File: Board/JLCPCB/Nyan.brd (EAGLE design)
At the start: 86 x 42 mm, 63 parts, among them IC1 74HCT541PW, IC2 STM32F10XCXT6, IC3 74HCT541PW, IC4 ST3485, U2 A4988_STEP, U3 MAX6966, X1 WR-WTB2.0-2_THT-VER, X10 32768, X2 WR-WTB2.0-4_THT_VER, X3 WR-WTB2.0-5_THT-VER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

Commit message: [Board] A little more layouting done
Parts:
- removed SV1: (no value), con-lstb:MA03-2
- added JP1, JP2: (no value), jumper:JP1
- moved LED1 32.3 mm to (54.2, 14.7), turned to 180 degrees
- moved R9 30.1 mm to (54.5, 17.9), turned to 90 degrees
- moved X9 28.9 mm to (24.1, 12.8), turned to 0 degrees
- moved C10 25.9 mm to (23.1, 16.2)
- moved C9 24.6 mm to (22.9, 9.65)
- moved X10 23.3 mm to (29.9, 11.1)
- moved C7 20.2 mm to (1.25, 2.60), flipped to the top
- moved C11 19.4 mm to (26.9, 8.20)
- moved C12 16.6 mm to (30.6, 8.40), turned to 0 degrees
- moved C18 14.4 mm to (50.0, 3.10)
- moved C16 14.4 mm to (45.0, 3.10)
- moved C17 14.4 mm to (47.4, 2.90)
- moved C19 13.8 mm to (52.0, 2.90)
- moved C15 13.8 mm to (42.5, 3.10)
- moved R5 13.3 mm to (2.90, 2.90), flipped to the top
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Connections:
- removed net N$12: R6.2, SV1.2
- removed net N$13: R7.2, SV1.1
- net +3V3: now also JP1.2, JP2.2; no longer SV1.5, SV1.6
- net BOOT1: now also JP2.1, R6.2; no longer SV1.4
- net N$7: now also JP1.1, R7.2; no longer SV1.3

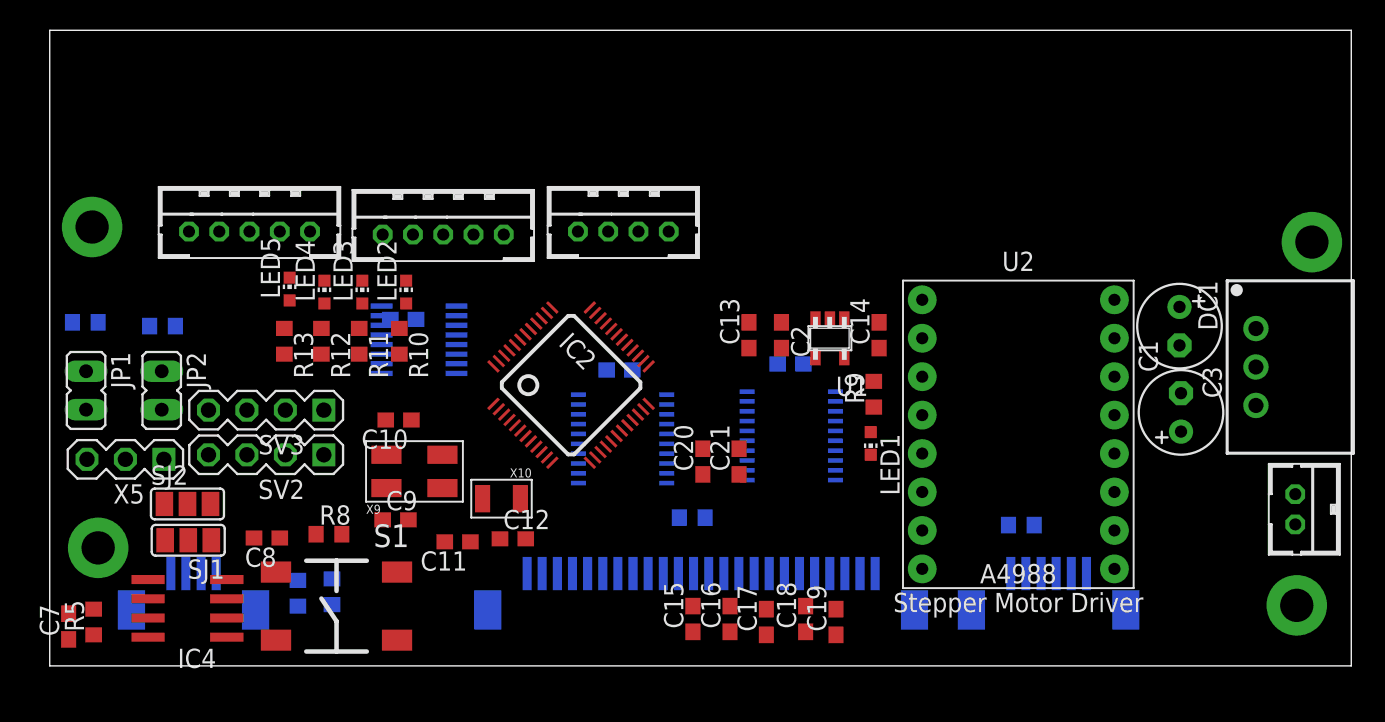
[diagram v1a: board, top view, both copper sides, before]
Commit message: [Board] Positioning done
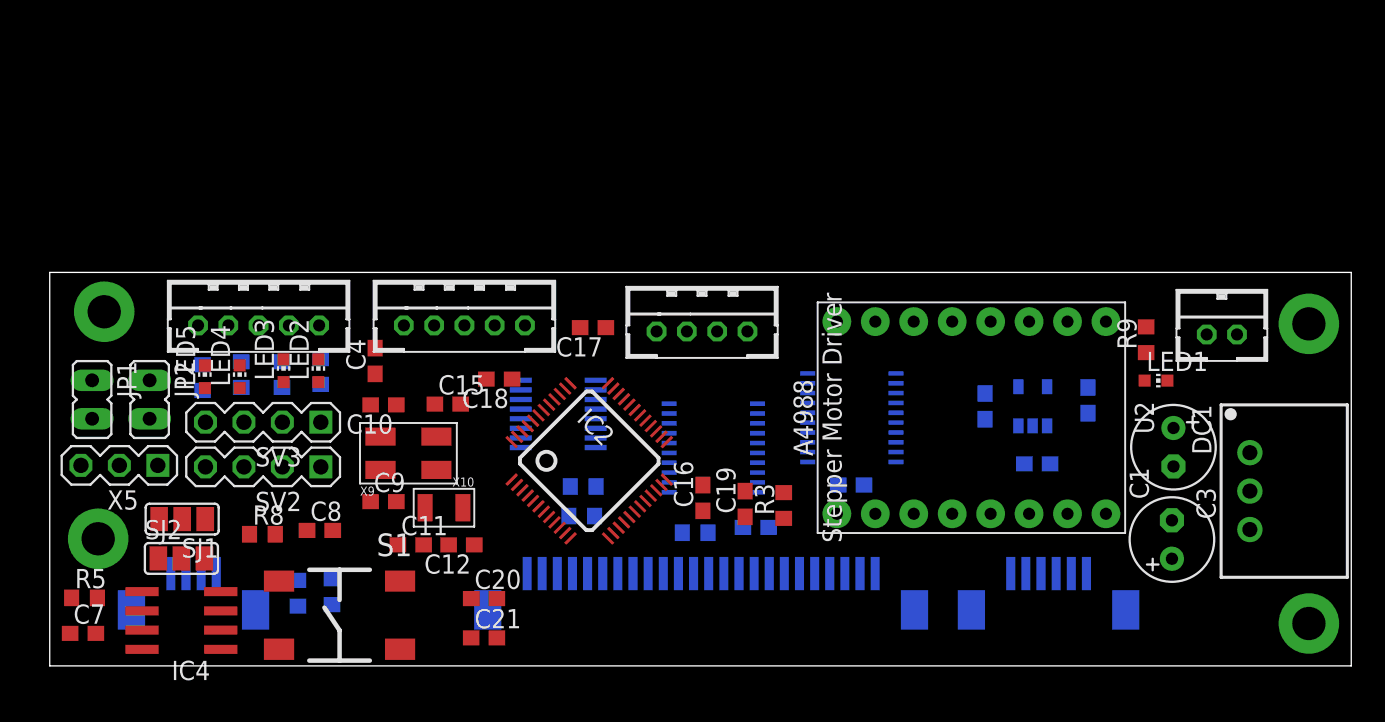
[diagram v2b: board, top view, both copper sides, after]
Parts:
- moved R7 35.2 mm to (35.1, 9.90)
- moved R6 29.8 mm to (35.2, 11.8)
- moved C18 25.7 mm to (29.7, 18.9), turned to 180 degrees
- moved C17 22.6 mm to (35.9, 22.4), turned to 180 degrees
- moved C15 21.5 mm to (26.3, 17.3), turned to 0 degrees
- moved C21 20.5 mm to (28.7, 1.85), turned to 0 degrees
- moved LED1 19.3 mm to (73.1, 18.9), turned to 270 degrees
- moved C2 18.9 mm to (65.2, 13.3), flipped to the bottom, turned to 0 degrees
- moved R9 18.4 mm to (72.5, 21.6)
- moved C20 17.1 mm to (28.7, 4.45), turned to 0 degrees
- moved C13 16.3 mm to (61.8, 17.1), flipped to the bottom, turned to 270 degrees
- moved R3 15.8 mm to (48.5, 10.6), flipped to the top, turned to 90 degrees
- moved X4 15.5 mm to (27.4, 22.5)
- moved C14 14.5 mm to (68.6, 17.6), flipped to the bottom, turned to 270 degrees
- moved U1 14.1 mm to (65.0, 17.1), flipped to the bottom, turned to 0 degrees
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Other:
- board size 86 x 42 mm -> 86 x 26 mm

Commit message: [Board] Fixed positions for half the components
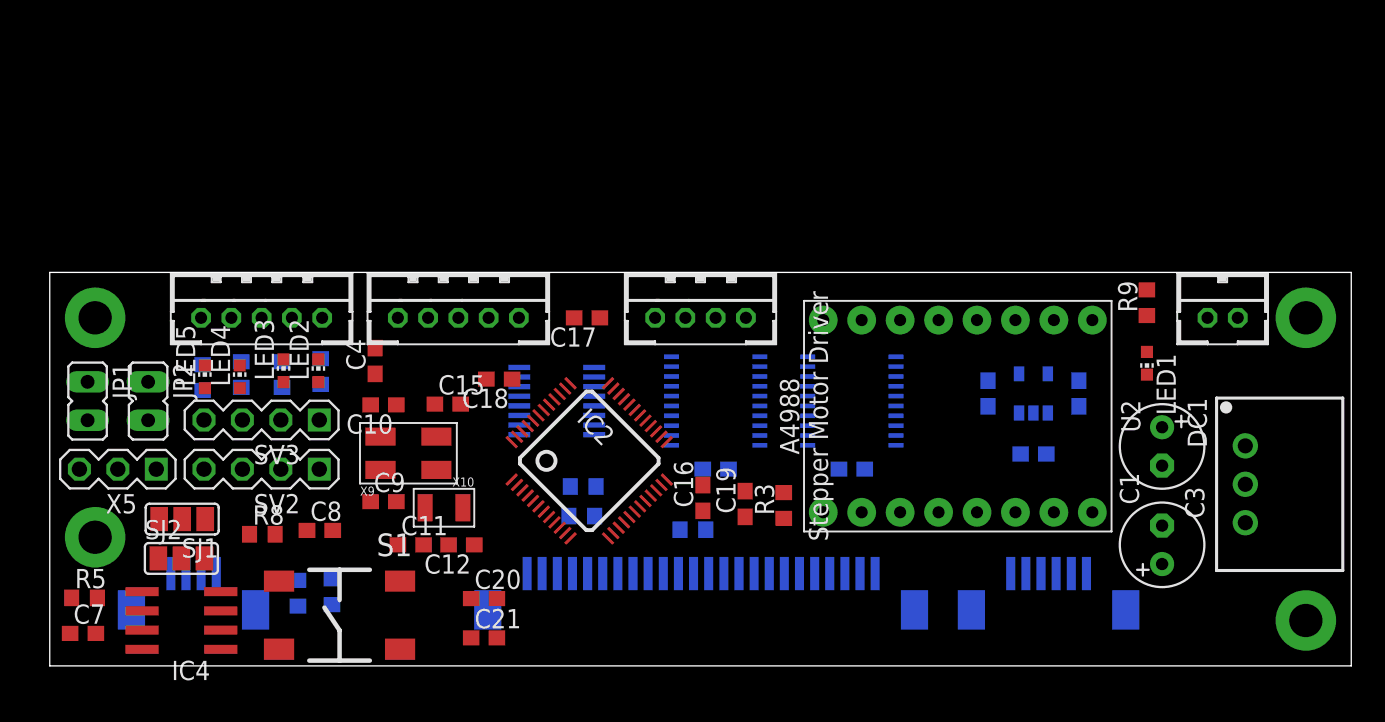
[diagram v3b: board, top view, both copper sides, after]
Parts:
- moved C5 4.67 mm to (44.0, 13.0)
- moved IC3 3.10 mm to (44.0, 17.5)
- moved R9 2.45 mm to (72.5, 24.0)
- moved LED1 1.30 mm to (72.5, 20.0), turned to 180 degrees
- moved X1 1.10 mm to (77.5, 23.0)
- moved IC1 1.10 mm to (53.0, 17.5)
- moved C6 1.05 mm to (53.0, 13.0)
- moved U2 0.91 mm to (60.0, 16.5)
- moved X2 0.91 mm to (43.0, 23.0)
- moved C13 0.87 mm to (62.0, 18.0)
- moved U3 0.86 mm to (33.5, 17.5)
- moved U1 0.85 mm to (65.0, 18.0)
- moved C17 0.76 mm to (35.5, 23.0)
- moved C3 0.75 mm to (73.5, 14.5)
- moved C14 0.75 mm to (68.0, 18.0)
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
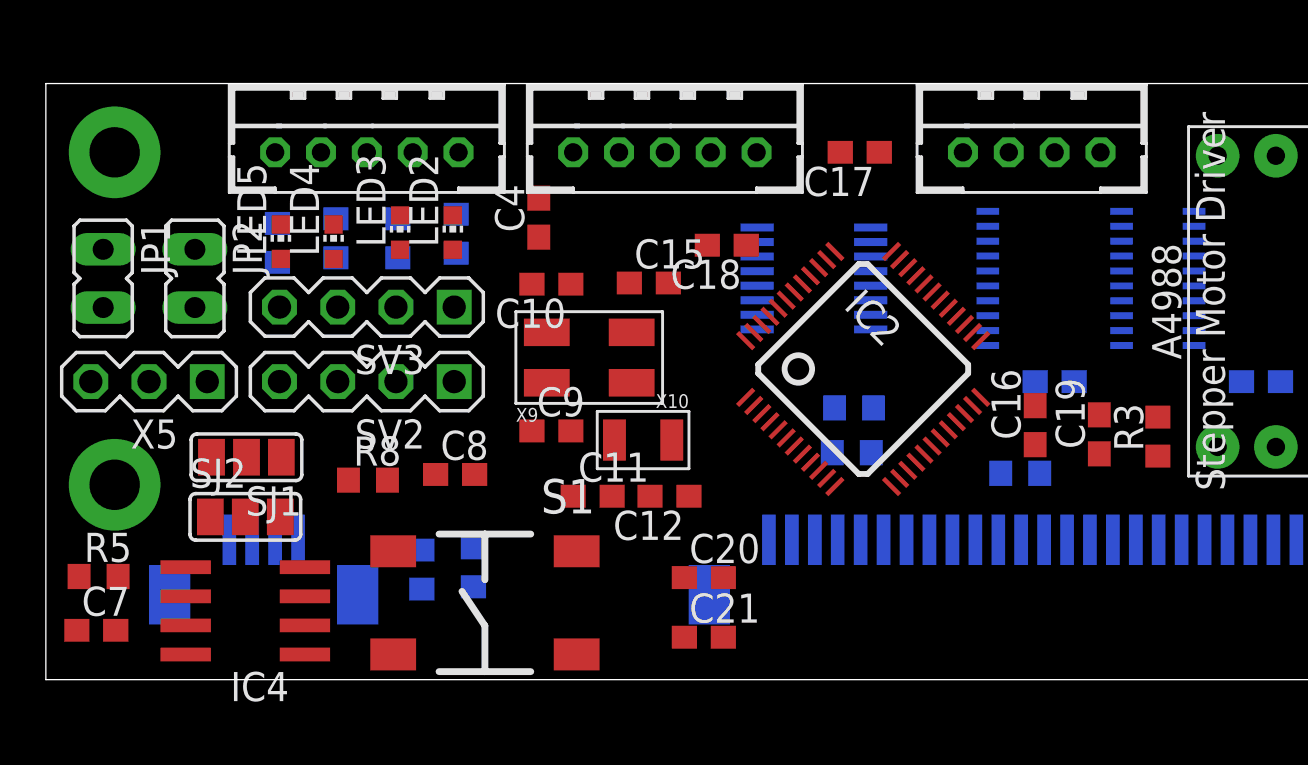
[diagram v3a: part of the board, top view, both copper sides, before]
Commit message: [Board] Fixed positioning done
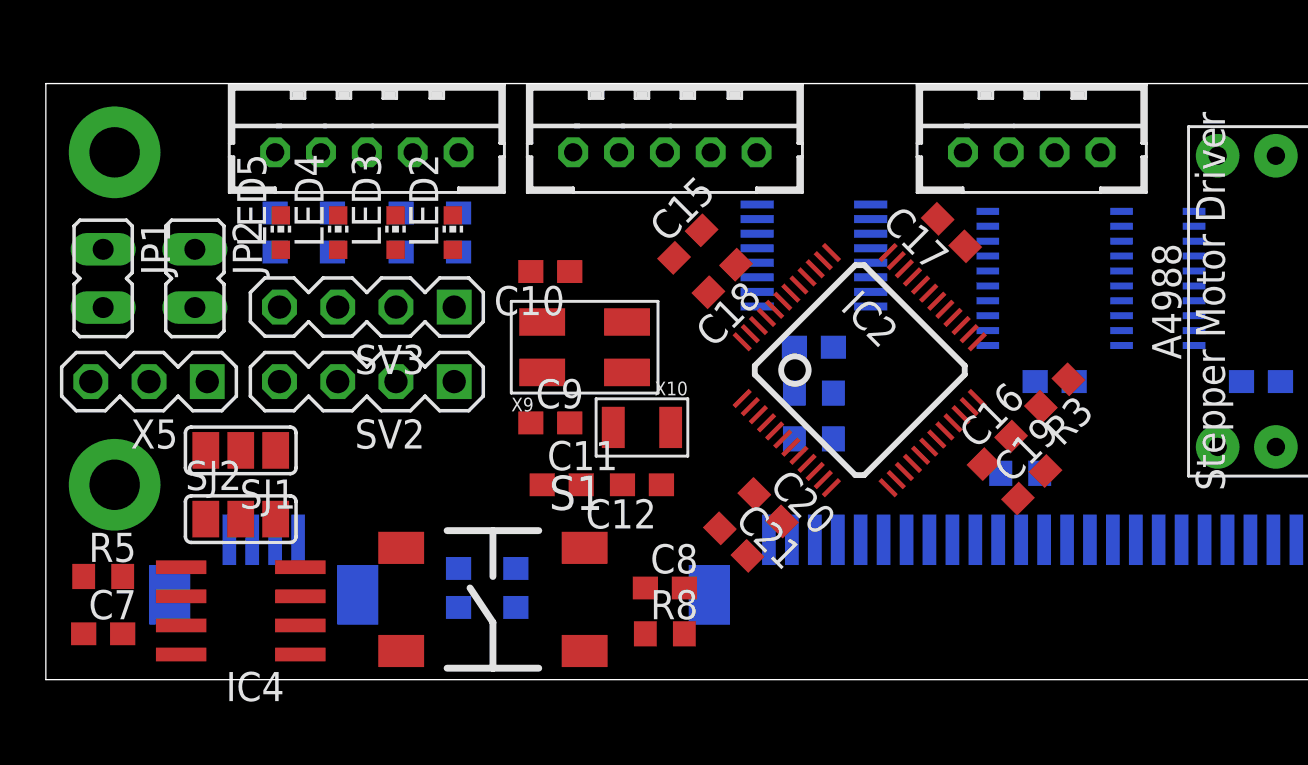
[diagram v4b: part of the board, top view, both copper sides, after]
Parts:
- moved R8 14.6 mm to (27.0, 2.00)
- moved C4 13.3 mm to (33.5, 14.5), flipped to the bottom, turned to 0 degrees
- moved C8 10.4 mm to (27.0, 4.00)
- moved C17 5.32 mm to (39.5, 19.5), turned to 135 degrees
- moved R3 4.88 mm to (44.0, 12.5), turned to 225 degrees
- moved C21 4.35 mm to (30.0, 6.00), turned to 315 degrees
- moved C20 4.14 mm to (31.5, 7.50), turned to 315 degrees
- moved C19 3.68 mm to (43.0, 8.50), turned to 45 degrees
- moved C15 2.40 mm to (28.0, 19.0), turned to 45 degrees
- moved R2 2.06 mm to (20.5, 4.00)
- moved C16 1.98 mm to (41.5, 10.0), turned to 45 degrees
- moved R6 1.87 mm to (33.5, 12.5)
- moved R1 1.79 mm to (18.0, 4.00)
- moved R7 1.76 mm to (33.5, 10.5)
- moved C18 1.46 mm to (29.5, 17.5), turned to 225 degrees
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
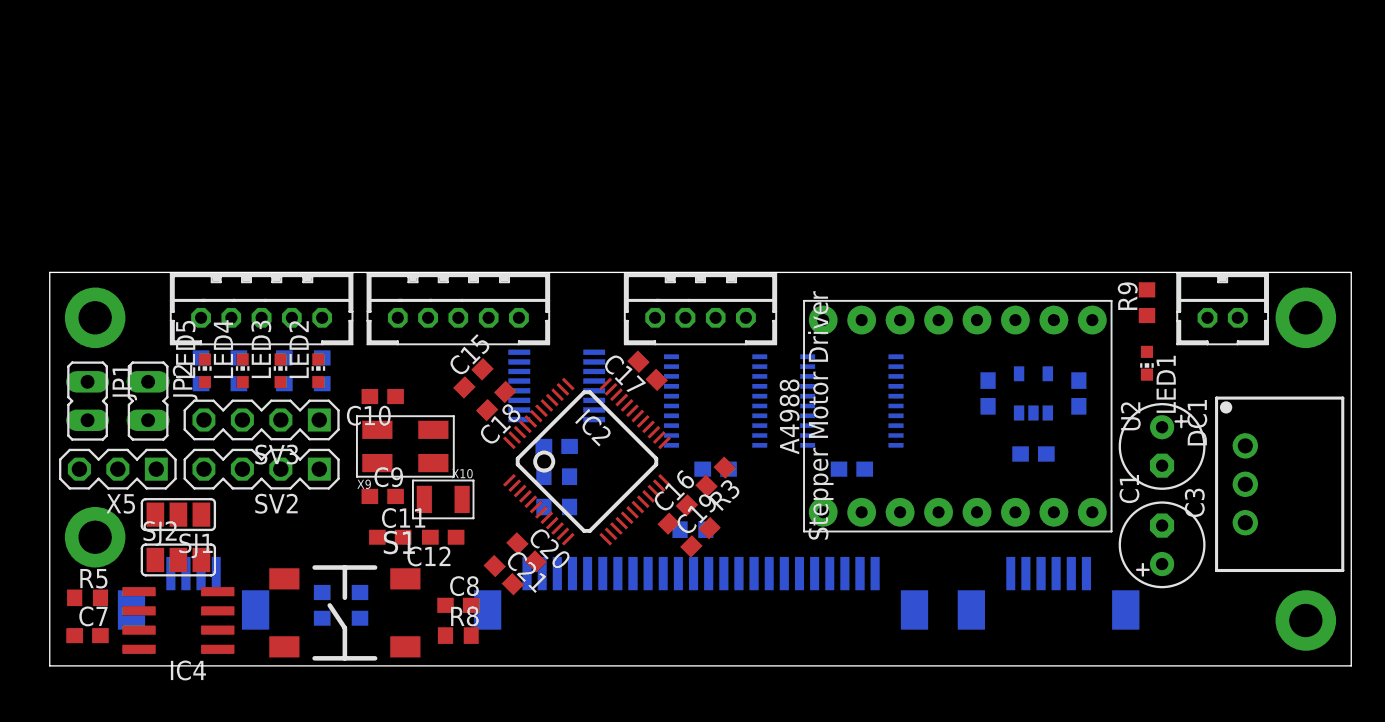
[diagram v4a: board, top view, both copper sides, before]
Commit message: [Board] Some progress in routing
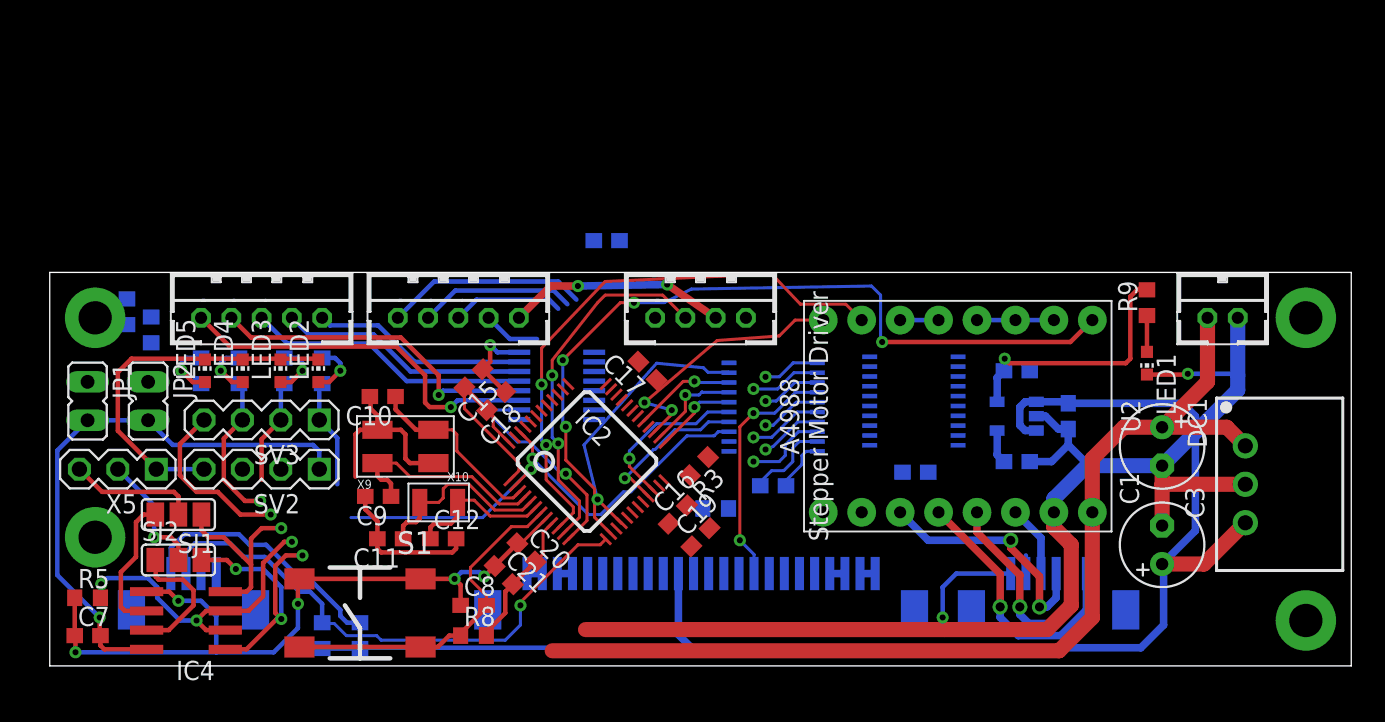
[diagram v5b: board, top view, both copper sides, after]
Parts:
- moved R7 31.2 mm to (5.10, 23.4), turned to 90 degrees
- moved R6 28.5 mm to (6.70, 22.2), turned to 90 degrees
- moved C4 14.0 mm to (36.8, 28.1), turned to 180 degrees
- moved C5 13.2 mm to (57.2, 12.8)
- moved IC3 13.1 mm to (57.1, 17.5)
- moved C6 5.32 mm to (47.8, 11.9)
- moved IC1 5.22 mm to (47.8, 17.1)
- moved C13 4.88 mm to (63.9, 13.5), turned to 180 degrees
- moved C14 4.37 mm to (63.9, 19.5), turned to 180 degrees
- moved C2 3.40 mm to (67.3, 16.5), turned to 270 degrees
- moved R1 3.20 mm to (20.5, 2.00)
- moved R2 3.20 mm to (18.0, 2.00)
- moved R4 2.05 mm to (44.0, 10.4)
- moved U1 1.86 mm to (63.9, 16.5), turned to 270 degrees
- moved R3 1.30 mm to (42.9, 13.2)
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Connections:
- net BUT_LED: now also U3.13; no longer U3.12
- net FREE_LED: now also U3.12; no longer U3.13
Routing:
- net GND: track 0.00 -> 207.3 mm, vias 0 -> 8
- net +5V: track 0.00 -> 115.6 mm, vias 0 -> 2
- net +3V3: track 0.00 -> 76.4 mm, vias 0 -> 2
- net +12V: track 0.00 -> 69.1 mm
- net MOT_EN: track 0.00 -> 53.5 mm, vias 0 -> 4
- net MOT_STP: track 0.00 -> 37.6 mm, vias 0 -> 2
- net PHOTO: track 0.00 -> 36.4 mm, vias 0 -> 1
- net LED1: track 0.00 -> 24.7 mm, vias 0 -> 1
- net BUT_SIG: track 0.00 -> 24.1 mm, vias 0 -> 2
- net N$8: track 0.00 -> 22.8 mm
- net LED2: track 0.00 -> 22.0 mm, vias 0 -> 1
- net PC13: track 0.00 -> 22.0 mm, vias 0 -> 1
- net RTS: track 0.00 -> 20.9 mm, vias 0 -> 3
- net D2: track 0.00 -> 18.9 mm, vias 0 -> 1
- net LED3: track 0.00 -> 18.8 mm
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
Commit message: [Board] Some more traces :)
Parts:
- moved R3 15.5 mm to (57.1, 7.10), flipped to the bottom, turned to 0 degrees
- moved C8 0.78 mm to (27.4, 4.50)
- moved R8 0.72 mm to (27.4, 2.40)
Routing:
- net PA7: track 9.93 -> 48.1 mm, vias 1 -> 4
- net PA5: track 6.97 -> 43.9 mm, vias 0 -> 4
- net MOT_THERM: track 1.20 -> 37.0 mm, vias 0 -> 1
- net PC13: track 22.0 -> 46.3 mm, vias 1 -> 4
- net HEAD_THERM: track 0.00 -> 19.3 mm, vias 0 -> 1
- net +12V: track 69.1 -> 79.3 mm, vias 0 -> 2
- net GND: track 207.3 -> 217.2 mm, vias 8 -> 10
- net N$8: track 22.8 -> 27.0 mm
- net BOOT1: track 0.00 -> 4.08 mm, vias 0 -> 1
- net +3V3: track 76.4 -> 80.3 mm
- net +5V: track 115.6 -> 117.8 mm
- net PA15: track 11.4 -> 12.9 mm
- net RX: track 18.4 -> 19.8 mm
- net RTS: track 20.9 -> 22.2 mm
- net PHOTO: track 36.4 -> 37.5 mm
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
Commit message: [Board] And even more traces
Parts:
- moved R8 1.70 mm to (29.1, 2.40)
- moved R1 1.00 mm to (19.5, 2.00)
- moved S1 0.95 mm to (19.6, 3.20)
- moved R2 0.60 mm to (17.4, 2.00)
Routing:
- net +3V3: track 80.3 -> 115.6 mm, vias 2 -> 4
- net PA15: track 12.9 -> 43.3 mm, vias 1 -> 2
- net BOOT1: track 4.08 -> 32.1 mm
- net RTS: track 22.2 -> 47.2 mm, vias 3 -> 4
- net RX: track 19.8 -> 43.9 mm, vias 3 -> 4
- net TX: track 13.4 -> 36.1 mm, vias 1 -> 2
- net N$7: track 0.00 -> 22.7 mm
- net HEAD_THERM: track 19.3 -> 0.78 mm, vias 1 -> 0
- net MOT_THERM: track 37.0 -> 20.2 mm
- net GND: track 217.2 -> 229.4 mm, vias 10 -> 9
- net SWCLK: track 0.00 -> 8.16 mm
- net SWDIO: track 0.00 -> 5.45 mm
- net N$8: track 27.0 -> 31.4 mm
- net LED1: track 24.7 -> 23.4 mm
- net LED2: track 22.0 -> 21.0 mm
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
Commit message: [Board] More layouting done
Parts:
- moved R6 1.26 mm to (6.30, 23.4), turned to 270 degrees
- moved R7 1.20 mm to (6.30, 23.4), flipped to the top, turned to 270 degrees
- moved C17 0.98 mm to (38.6, 19.9)
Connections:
- net N$7 renamed BOOT0
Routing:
- net GND: track 229.4 -> 261.5 mm, vias 9 -> 12
- net LATCH: track 0.00 -> 27.6 mm, vias 0 -> 1
- net MOT_STP: track 37.9 -> 11.2 mm, vias 2 -> 0
- net +3V3: track 115.6 -> 129.9 mm, vias 4 -> 6
- net D2: track 18.9 -> 5.70 mm, vias 1 -> 0
- net BUT_SIG: track 24.1 -> 13.2 mm, vias 2 -> 0
- net MOT_EN: track 53.5 -> 43.7 mm, vias 4 -> 1
- net BOOT0: track 22.7 -> 28.8 mm
- net SWDIO: track 5.45 -> 11.1 mm, vias 0 -> 1
- net DCLK: track 6.80 -> 11.2 mm
- net BOOT1: track 32.1 -> 35.9 mm
- net LED_MOSI: track 0.00 -> 3.76 mm, vias 0 -> 1
- net LED4: track 16.5 -> 19.9 mm, vias 0 -> 2
- net MOT_DIR: track 17.6 -> 14.3 mm, vias 2 -> 0
- net LED_MISO: track 0.00 -> 3.23 mm, vias 0 -> 1
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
